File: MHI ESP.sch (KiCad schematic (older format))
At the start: 9 parts, among them J1 , U1 WeMos_D1_mini, U2 R-78E5.0-1.0, U3 DS18B20U, U4 TXB0104PW

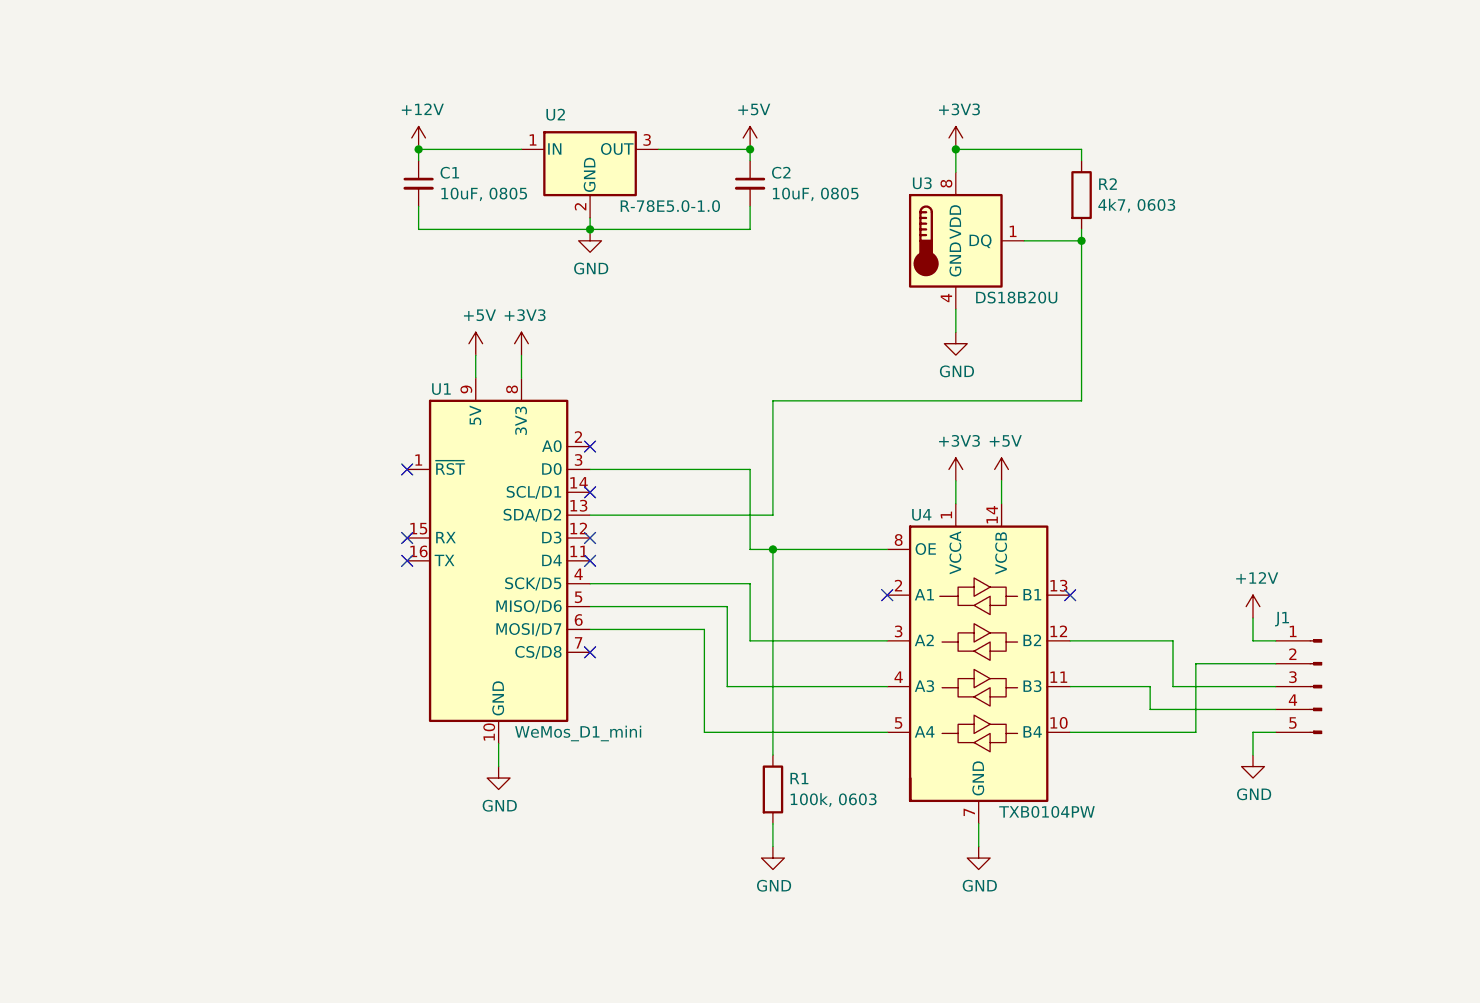
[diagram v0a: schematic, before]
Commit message: Remove TXB0104 IC, DS18B20 IC and change 5V IC
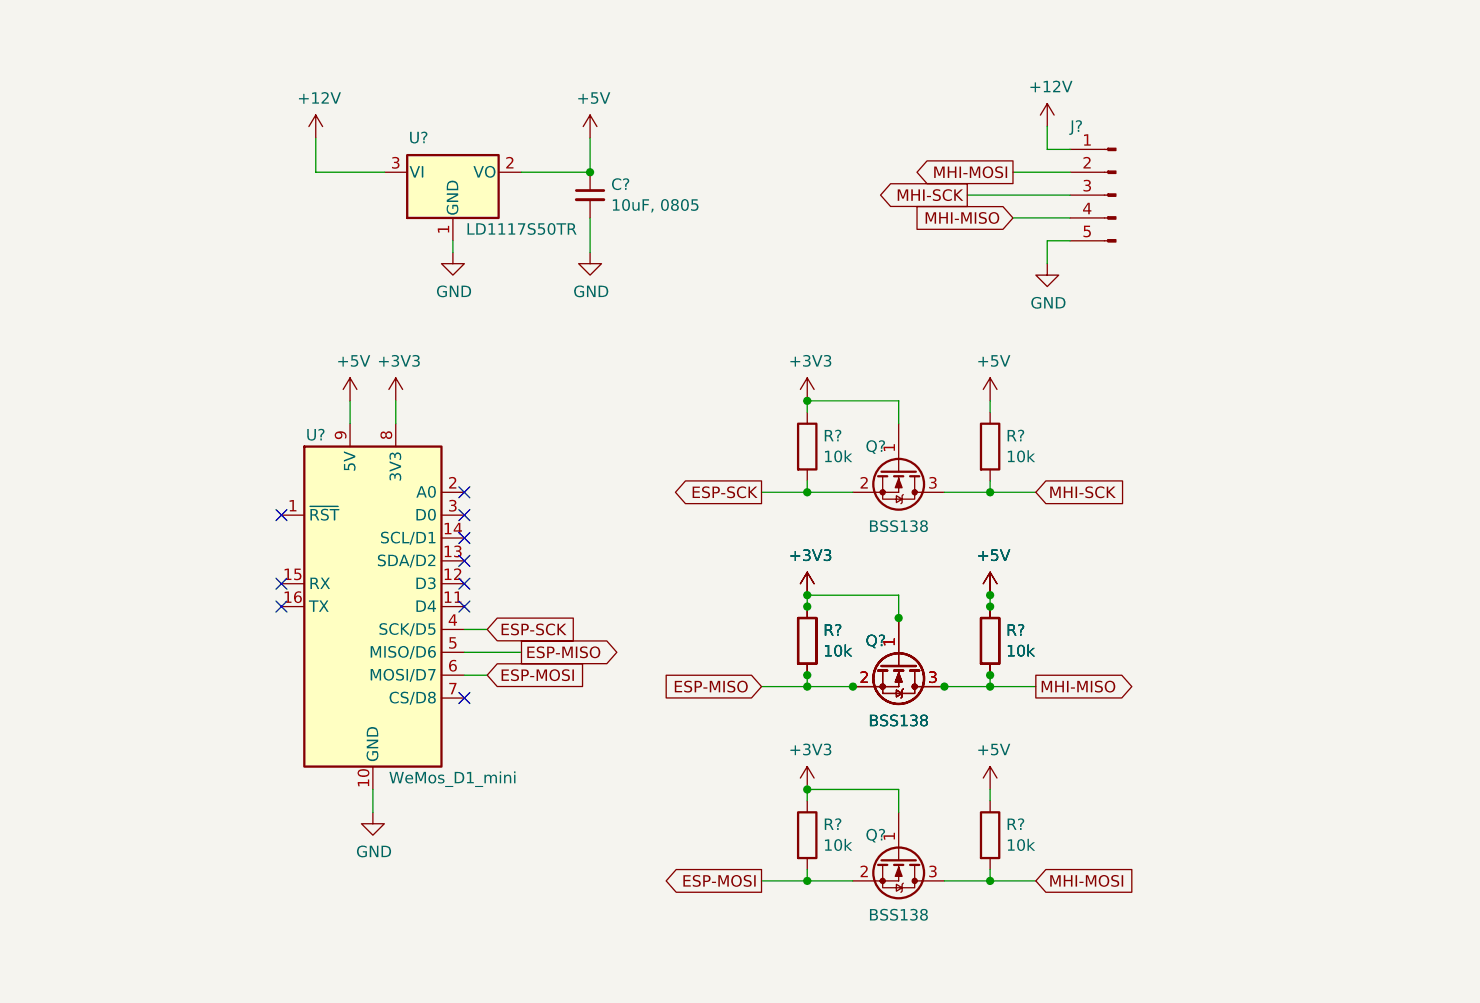
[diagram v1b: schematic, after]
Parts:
- removed C1: 10uF, 0805, Capacitor_SMD:C_0805_2012Metric, symbol Device:C_Small
- removed R1: 100k, 0603, Resistor_SMD:R_0603_1608Metric, symbol Device:R
- removed R2: 4k7, 0603, Resistor_SMD:R_0603_1608Metric, symbol Device:R
- removed U2: R-78E5.0-1.0, Converter_DCDC:Converter_DCDC_RECOM_R-78E-0.5_THT, symbol Regulator_Switching:R-78E5.0-1.0
- removed U3: DS18B20U, Package_SO:MSOP-8_3x3mm_P0.65mm, symbol Sensor_Temperature:DS18B20U
- removed U4: TXB0104PW, Package_SO:TSSOP-14_4.4x5mm_P0.65mm, symbol Logic_LevelTranslator:TXB0104PW
- added Q? (x4): BSS138, Package_TO_SOT_SMD:SOT-23, symbol Transistor_FET:BSS138
- added R? (x8): 10k, Resistor_SMD:R_0805_2012Metric, symbol Device:R
- added U?: LD1117S50TR, Package_TO_SOT_SMD:SOT-223-3_TabPin2, symbol Regulator_Linear:LD1117S50TR_SOT223
- renumbered C2 to C?, J1 to J?, U1 to U?
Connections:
- net +12V: now also U?.3 (VI)
- net +3V3: now also Q?.1 (G), Q?.1 (G), Q?.1 (G), Q?.1 (G), R?.1, R?.1, R?.1, R?.1
- net +5V: now also R?.1, R?.1, R?.1, R?.1, U?.2 (VO)
- net GND: now also U?.1 (GND)
- net ESP-SCK: now reaches U?.4 (SCK/D5)
- net ESP-SCK: now also Q?.2 (S), R?.2
- net ESP-MISO: now reaches U?.5 (MISO/D6)
- net ESP-MISO: now also Q?.2 (S), Q?.2 (S), R?.2, R?.2
- net ESP-MOSI: now reaches U?.6 (MOSI/D7)
- net ESP-MOSI: now also Q?.2 (S), R?.2
- net MHI-MOSI: now reaches J?.2 (Pin_2)
- net MHI-MOSI: now also Q?.3 (D), R?.2
- net MHI-MISO: now reaches J?.4 (Pin_4)
- net MHI-MISO: now also Q?.3 (D), Q?.3 (D), R?.2, R?.2
- net MHI-SCK: now reaches J?.3 (Pin_3)
- net MHI-SCK: now also Q?.3 (D), R?.2
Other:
- moved on the sheet: C?, J?, U?

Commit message: Re-annotate schematic and update components on PCB, ready for new track layout
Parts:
- removed Q?: BSS138, Package_TO_SOT_SMD:SOT-23, symbol Transistor_FET:BSS138
- removed R? (x2): 10k, Resistor_SMD:R_0805_2012Metric, symbol Device:R
- gave numbers to parts that had none: 13

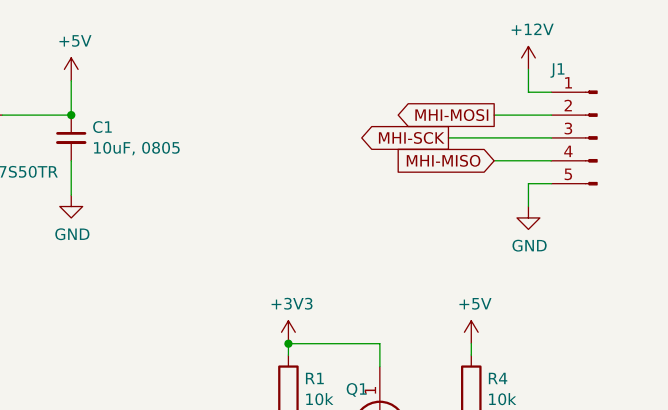
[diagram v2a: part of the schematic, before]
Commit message: Update connector footprint to 05JQ-BT to accomodate non-cabled installs
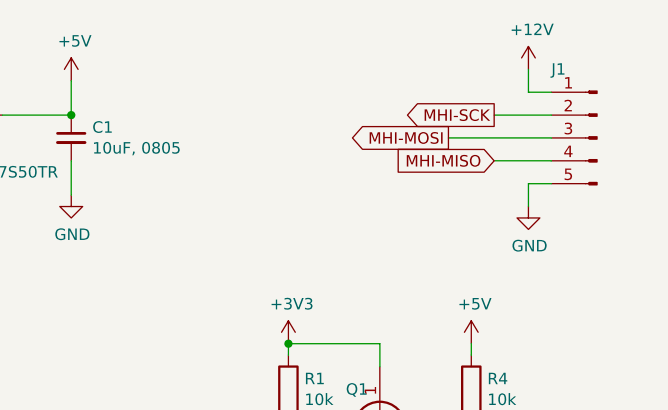
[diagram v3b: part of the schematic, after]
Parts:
- J1: footprint Connector_PinHeader_2.54mm:PinHeader_1x05_P2.54mm_Vertical -> Connector_JST:JST_XH_B5B-XH-A_1x05_P2.50mm_Vertical
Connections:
- net MHI-MOSI: now also J1.3 (Pin_3); no longer J1.2 (Pin_2)
- net MHI-SCK: now also J1.2 (Pin_2); no longer J1.3 (Pin_3)
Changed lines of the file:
@@
 F 0 "J1" H 7550 2600 50  0000 R CNN
 F 1 " " H 7322 2233 50  0000 R CNN
-F 2 "Connector_PinHeader_2.54mm:PinHeader_1x05_P2.54mm_Vertical" H 7350 2300 50  0001 C CNN
+F 2 "Connector_JST:JST_XH_B5B-XH-A_1x05_P2.50mm_Vertical" H 7350 2300 50  0001 C CNN
 F 3 "~" H 7350 2300 50  0001 C CNN
 	1    7350 2300
@@
 Text GLabel 4600 4400 2    50   Input ~ 0
 ESP-MOSI
-Text GLabel 6700 2300 0    50   Output ~ 0
+Text GLabel 6900 2200 0    50   Output ~ 0
 MHI-SCK
 Text GLabel 6900 2400 0    50   Input ~ 0
 MHI-MISO
-Text GLabel 6900 2200 0    50   Output ~ 0
+Text GLabel 6700 2300 0    50   Output ~ 0
 MHI-MOSI
 Wire Wire Line

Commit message: Start of IR data capturing idea...
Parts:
- added J2: DISPLAY, Connector_JST:JST_XH_B8B-XH-A_1x08_P2.50mm_Vertical, symbol Connector:Conn_01x08_Male
- added J3: CNE, Connector_JST:JST_XH_B8B-XH-A_1x08_P2.50mm_Vertical, symbol Connector:Conn_01x08_Male
- J1: value (none) -> CNS
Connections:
- new net: J2.1 (Pin_1), J3.1 (Pin_1)
- new net: J2.2 (Pin_2), J3.2 (Pin_2)
- new net: J2.3 (Pin_3), J3.3 (Pin_3)
- new net: J2.4 (Pin_4), J3.4 (Pin_4)
- new net: J2.5 (Pin_5), J3.5 (Pin_5)
- new net: J2.7 (Pin_7), J3.7 (Pin_7)
- new net: J2.8 (Pin_8), J3.8 (Pin_8)
- new net IRDIN: J2.6 (Pin_6)
- new net IRDOUT: J3.6 (Pin_6)
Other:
- moved on the sheet: C1, J1, Q1, Q2, Q3, R1, R2, R3, R4, R5, R6, U1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

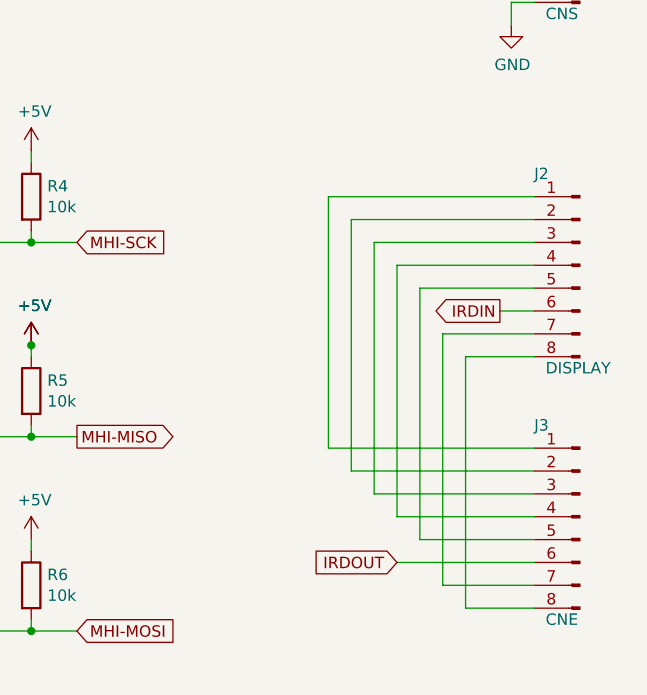
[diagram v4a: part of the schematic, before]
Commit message: Reconfigured J2 and J3 to suit cable out to CNE.
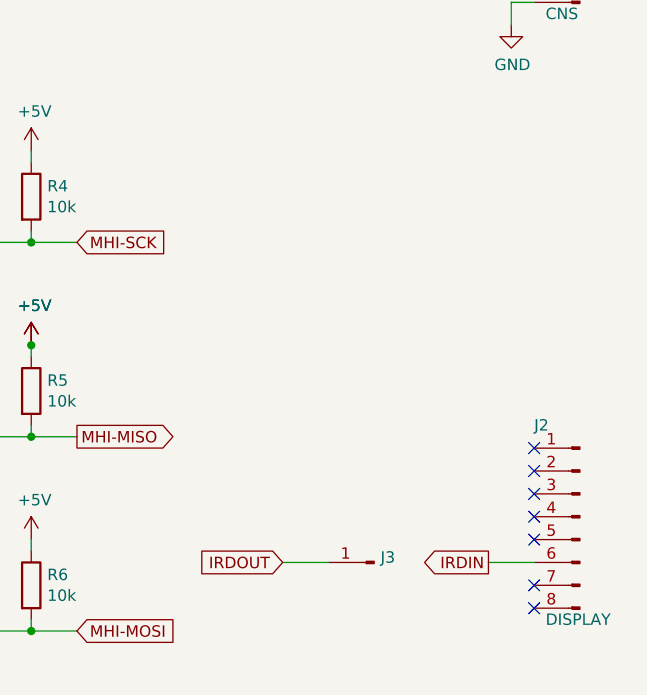
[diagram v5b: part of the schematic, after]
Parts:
- removed J2: DISPLAY, Connector_JST:JST_XH_B8B-XH-A_1x08_P2.50mm_Vertical, symbol Connector:Conn_01x08_Male
- added J3: Conn_01x01_Male, Connector_Pin:Pin_D1.0mm_L10.0mm, symbol Connector:Conn_01x01_Male
- J2: renamed from J3; value CNE -> DISPLAY
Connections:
- net IRDIN: now also J2.6 (Pin_6)
- net IRDOUT: now also J3.1 (Pin_1); no longer J2.6 (Pin_6)
- no-connect marks 10 -> 17
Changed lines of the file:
@@
 	1    0    0    -1
-$EndComp
-$Comp
-L Connector:Conn_01x08_Male J2
-U 1 1 613EA0E2
-P 8350 3700
-F 0 "J2" H 8550 4100 50  0000 R CNN
-F 1 "DISPLAY" H 8500 3250 50  0000 R CNN
-F 2 "Connector_JST:JST_XH_B8B-XH-A_1x08_P2.50mm_Vertical" H 8350 3700 50  0001 C CNN
-F 3 "~" H 8350 3700 50  0001 C CNN
-	1    8350 3700
-	-1   0    0    -1
 $EndComp
 Wire Wire Line
@@
 $EndComp
 Connection ~ 5950 4050
+Text GLabel 7950 5000 0    50   Output ~ 0
+IRDIN
+Text GLabel 7050 5000 0    50   Input ~ 0
+IRDOUT
 $Comp
-L Connector:Conn_01x08_Male J3
+L Connector:Conn_01x08_Male J2
 U 1 1 613E9E86
 P 8350 4800
-F 0 "J3" H 8550 5200 50  0000 R CNN
-F 1 "CNE" H 8500 4350 50  0000 R CNN
+F 0 "J2" H 8550 5200 50  0000 R CNN
+F 1 "DISPLAY" H 8500 4350 50  0000 R CNN
 F 2 "Connector_JST:JST_XH_B8B-XH-A_1x08_P2.50mm_Vertical" H 8350 4800 50  0001 C CNN
 F 3 "~" H 8350 4800 50  0001 C CNN
@@
 $EndComp
 Wire Wire Line
-	7850 5200 7850 4100
+	7950 5000 8150 5000
+NoConn ~ 8150 4500
+NoConn ~ 8150 4600
+NoConn ~ 8150 4700
+NoConn ~ 8150 4800
+NoConn ~ 8150 4900
+NoConn ~ 8150 5100
+NoConn ~ 8150 5200
+$Comp
+L Connector:Conn_01x01_Male J3
+U 1 1 614048E7
+P 7450 5000
+F 0 "J3" H 7422 4978 50  0000 R CNN
+F 1 "Conn_01x01_Male" H 7422 5023 50  0001 R CNN
+F 2 "Connector_Pin:Pin_D1.0mm_L10.0mm" H 7450 5000 50  0001 C CNN
+F 3 "~" H 7450 5000 50  0001 C CNN
+	1    7450 5000
+	-1   0    0    1
+$EndComp
 Wire Wire Line
-	7850 4100 8150 4100
-Wire Wire Line
-	7850 5200 8150 5200
-Wire Wire Line
-	7750 4000 7750 5100
-Wire Wire Line
-	7750 5100 8150 5100
-Wire Wire Line
-	7750 4000 8150 4000
-Wire Wire Line
-	7650 3800 7650 4900
-Wire Wire Line
-	7650 4900 8150 4900
-Wire Wire Line
-	7650 3800 8150 3800
-Wire Wire Line
-	7550 3700 7550 4800
-Wire Wire Line
-	7550 4800 8150 4800
-Wire Wire Line
-	7550 3700 8150 3700
-Wire Wire Line
-	7450 3600 7450 4700
-Wire Wire Line
-	7450 4700 8150 4700
-Wire Wire Line
-	7450 3600 8150 3600
-Wire Wire Line
-	7350 3500 7350 4600
-Wire Wire Line
-	7350 4600 8150 4600
-Wire Wire Line
-	7350 3500 8150 3500
-Wire Wire Line
-	7250 3400 7250 4500
-Wire Wire Line
-	7250 4500 8150 4500
-Wire Wire Line
-	7250 3400 8150 3400
-Text GLabel 8000 3900 0    50   Output ~ 0
-IRDIN
-Wire Wire Line
-	8000 3900 8150 3900
-Text GLabel 7550 5000 0    50   Input ~ 0
-IRDOUT
-Wire Wire Line
-	7550 5000 8150 5000
+	7050 5000 7250 5000
 $EndSCHEMATC

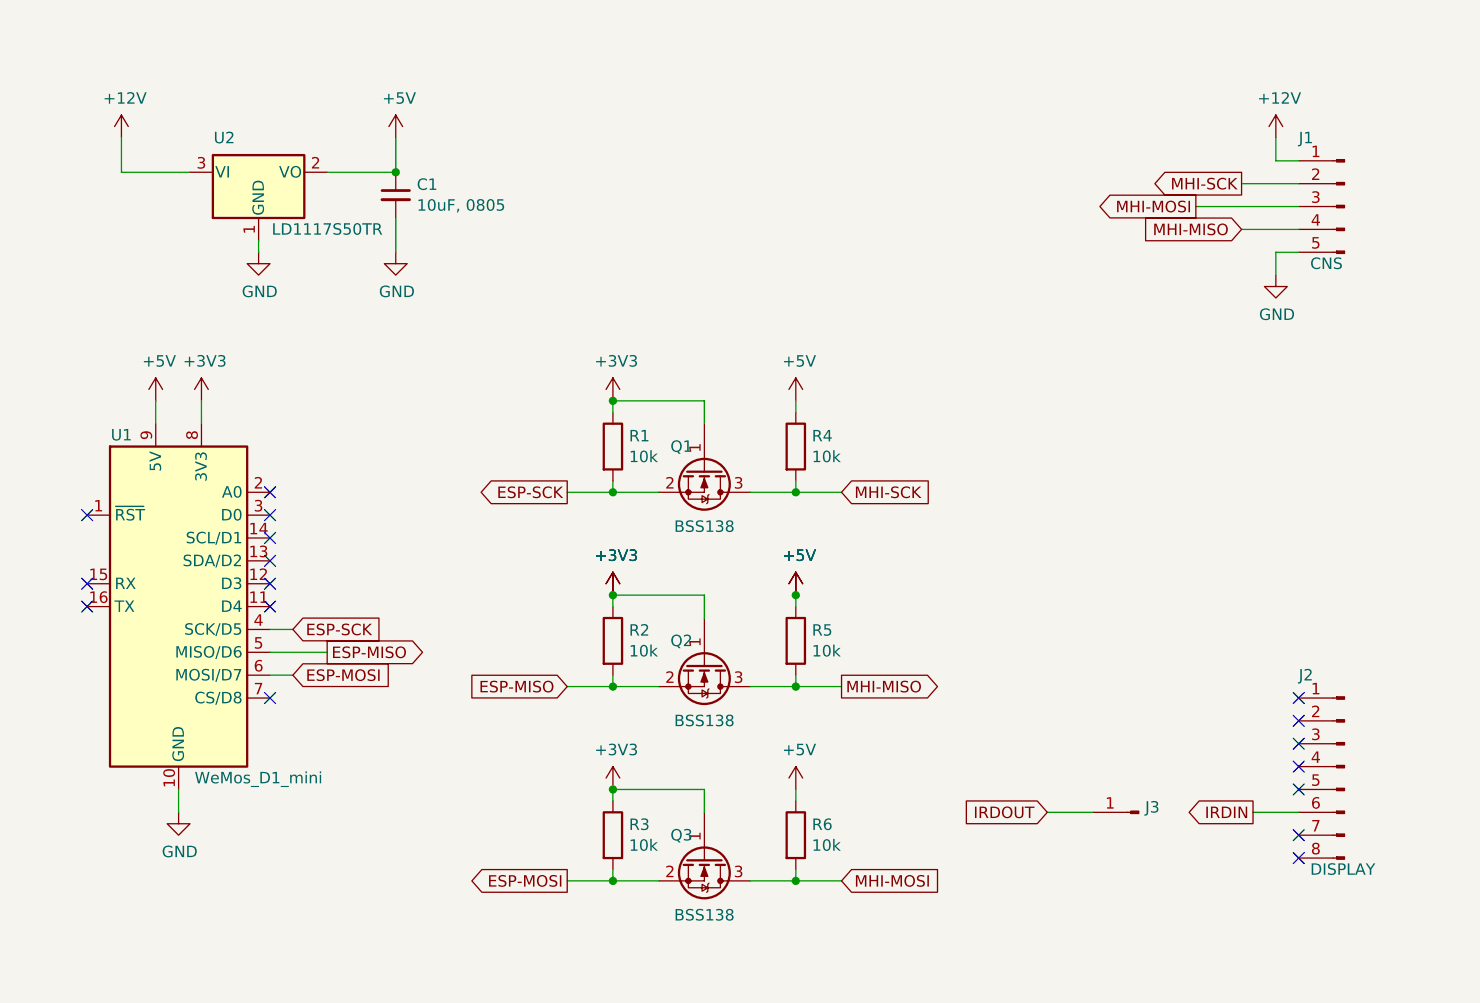
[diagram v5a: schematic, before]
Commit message: Added IR data injection circuit and headers
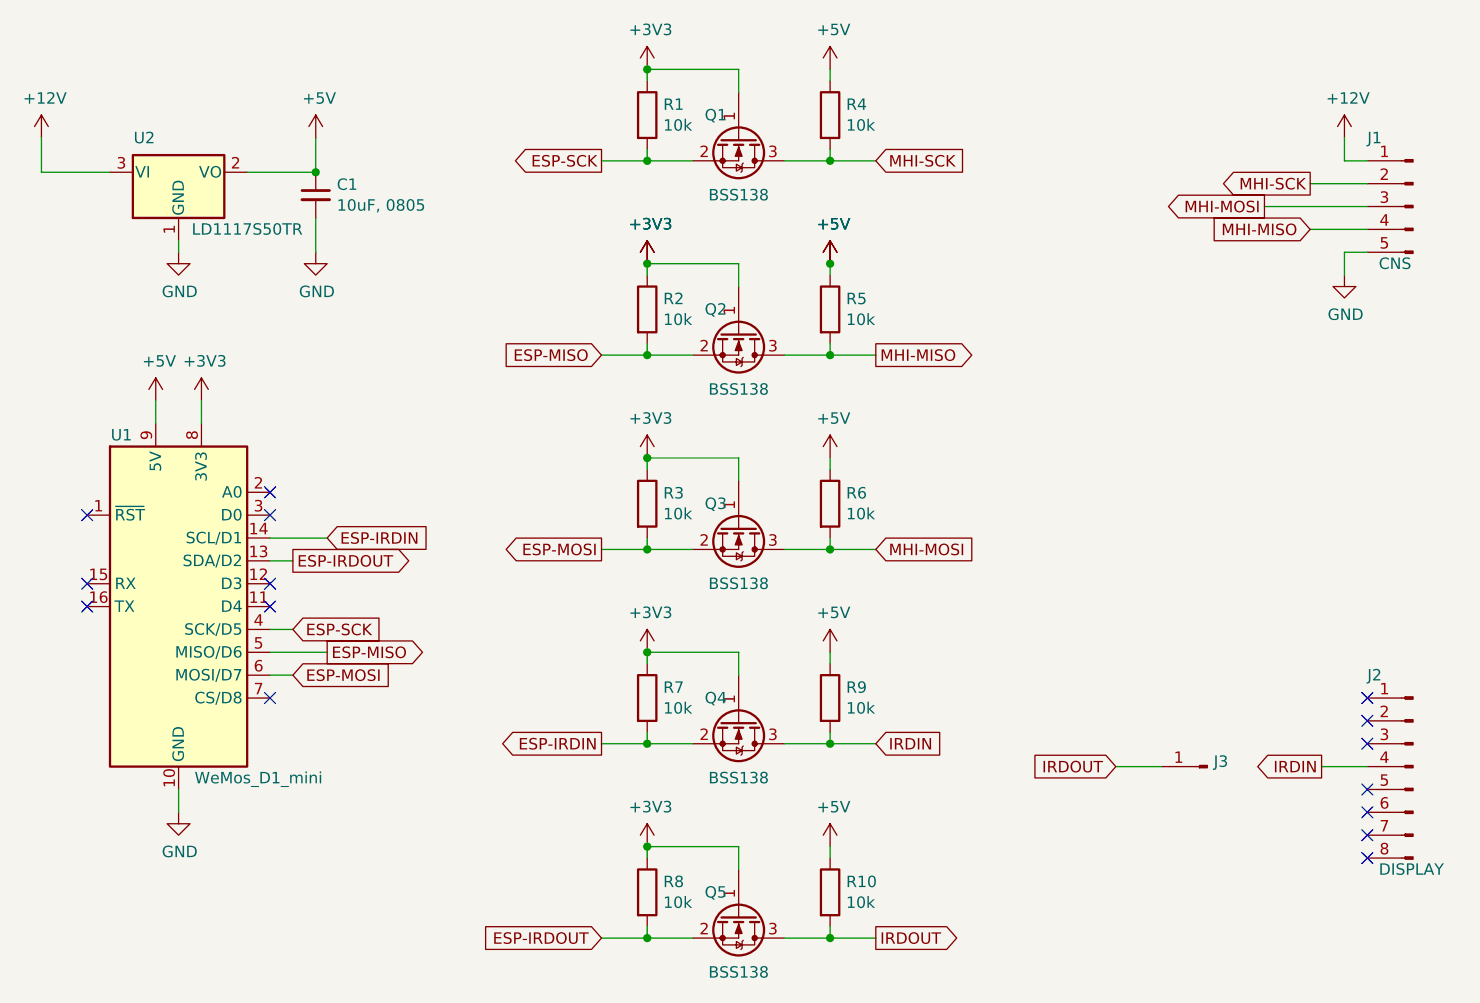
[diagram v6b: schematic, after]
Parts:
- added Q4, Q5: BSS138, Package_TO_SOT_SMD:SOT-23, symbol Transistor_FET:BSS138
- added R10, R7, R8, R9: 10k, Resistor_SMD:R_0805_2012Metric, symbol Device:R
- J2: footprint Connector_JST:JST_XH_B8B-XH-A_1x08_P2.50mm_Vertical -> Connector_JST:JST_XH_S8B-XH-A-1_1x08_P2.50mm_Horizontal
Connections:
- net +3V3: now also Q4.1 (G), Q5.1 (G), R7.1, R8.1
- net +5V: now also R10.1, R9.1
- net IRDIN: now also J2.4 (Pin_4), Q4.3 (D), R9.2; no longer J2.6 (Pin_6)
- net IRDOUT: now also Q5.3 (D), R10.2
- net ESP-IRDOUT: now reaches U1.13 (SDA/D2)
- net ESP-IRDOUT: now also Q5.2 (S), R8.2
- net ESP-IRDIN: now reaches U1.14 (SCL/D1)
- net ESP-IRDIN: now also Q4.2 (S), R7.2
- no-connect marks 17 -> 15
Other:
- moved on the sheet: C1, J1, J2, J3, Q1, Q2, Q3, R1, R2, R3, R4, R5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
